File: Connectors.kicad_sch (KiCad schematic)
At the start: 4 parts, among them J1 Conn_01x04_Pin, J2 Conn_01x04_Pin, J3 Conn_01x09_Pin, J4 Conn_02x03_Odd_Even

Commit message: Associated footprints to Symbols
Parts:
- J1, J2: footprint (none) -> Connector_PinHeader_2.54mm:PinHeader_1x04_P2.54mm_Vertical
- J3: footprint (none) -> Connector_PinHeader_2.54mm:PinHeader_1x09_P2.54mm_Vertical
- J4: footprint (none) -> Connector_PinHeader_2.54mm:PinHeader_2x03_P2.54mm_Vertical
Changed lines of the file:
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@@
 			)
 		)
-		(property "Footprint" ""
+		(property "Footprint" "Connector_PinHeader_2.54mm:PinHeader_1x04_P2.54mm_Vertical"
 			(at 129.54 57.15 0)
 			(effects
@@
 			)
 		)
-		(property "Footprint" ""
+		(property "Footprint" "Connector_PinHeader_2.54mm:PinHeader_2x03_P2.54mm_Vertical"
 			(at 95.25 106.68 0)
 			(effects
@@
 			)
 		)
-		(property "Footprint" ""
+		(property "Footprint" "Connector_PinHeader_2.54mm:PinHeader_1x04_P2.54mm_Vertical"
 			(at 109.22 74.93 0)
 			(effects
@@
 			)
 		)
-		(property "Footprint" ""
+		(property "Footprint" "Connector_PinHeader_2.54mm:PinHeader_1x09_P2.54mm_Vertical"
 			(at 161.29 96.52 0)
 			(effects

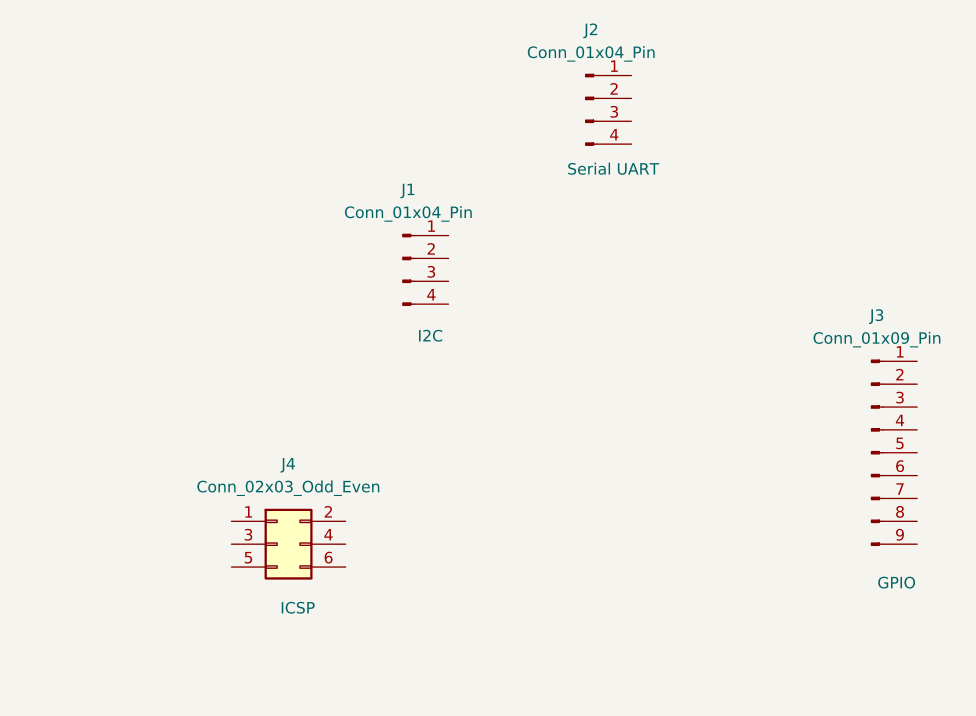
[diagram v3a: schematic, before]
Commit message: Completed wiring on second sheet and introduced hierarchial nets
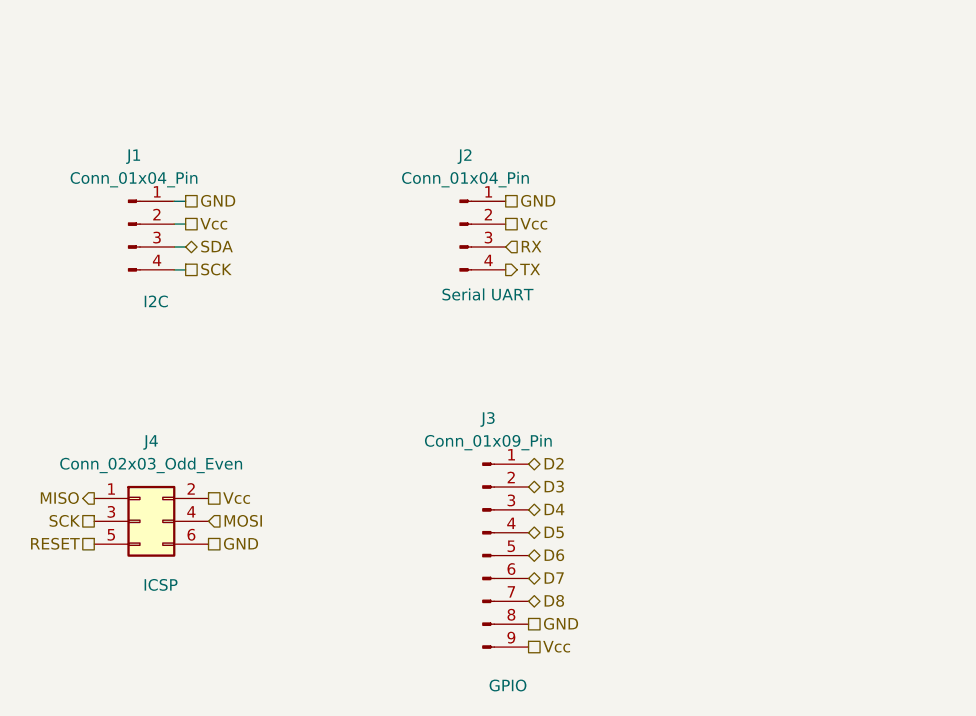
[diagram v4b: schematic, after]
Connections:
- net GND: now reaches J2.1 (Pin_1)
- net GND: now also J1.1 (Pin_1), J3.8 (Pin_8), J4.6 (Pin_6)
- net Vcc: now reaches J2.2 (Pin_2)
- net Vcc: now also J1.2 (Pin_2), J3.9 (Pin_9), J4.2 (Pin_2)
- net RX: now reaches J2.3 (Pin_3)
- net TX: now reaches J2.4 (Pin_4)
- net MISO: now reaches J4.1 (Pin_1)
- net SCK: now reaches J4.3 (Pin_3)
- net SCK: now also J1.4 (Pin_4)
- net MOSI: now reaches J4.4 (Pin_4)
- net RESET: now reaches J4.5 (Pin_5)
- net SDA: now reaches J1.3 (Pin_3)
- net D2: now reaches J3.1 (Pin_1)
- net D3: now reaches J3.2 (Pin_2)
- net D4: now reaches J3.3 (Pin_3)
- net D5: now reaches J3.4 (Pin_4)
- net D6: now reaches J3.5 (Pin_5)
- net D7: now reaches J3.6 (Pin_6)
- net D8: now reaches J3.7 (Pin_7)
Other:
- moved on the sheet: J1, J2, J3, J4
